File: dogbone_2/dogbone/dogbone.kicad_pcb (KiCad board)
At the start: 2 copper layers, 23 x 27.4 mm, 11 parts, among them J1 jstsh5x1, U1 TLV2771CDBVT

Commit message: added more to the mainboard/daugher board
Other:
- board text added: "ALT"
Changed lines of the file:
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@@
   (general
     (thickness 1.6)
-    (drawings 4)
+    (drawings 5)
     (tracks 53)
     (zones 0)
@@
     (37 F.SilkS user)
     (38 B.Mask user)
-    (39 F.Mask user hide)
+    (39 F.Mask user)
     (40 Dwgs.User user)
     (41 Cmts.User user)
@@
       (effects (font (size 1 1) (thickness 0.15)) (justify mirror))
     )
+    (fp_line (start -4.805 -6.84) (end 3.185 -6.84) (layer Dwgs.User) (width 0.12))
+    (fp_line (start -4.805 -6.84) (end -4.805 -3) (layer Dwgs.User) (width 0.12))
+    (fp_line (start 3.185 -3) (end -4.805 -3) (layer Dwgs.User) (width 0.12))
     (fp_line (start 3.185 -3) (end 3.185 -6.84) (layer Dwgs.User) (width 0.12))
-    (fp_line (start 3.185 -3) (end -4.805 -3) (layer Dwgs.User) (width 0.12))
-    (fp_line (start -4.805 -6.84) (end -4.805 -3) (layer Dwgs.User) (width 0.12))
-    (fp_line (start -4.805 -6.84) (end 3.185 -6.84) (layer Dwgs.User) (width 0.12))
     (pad 5 smd rect (at 1.19 -2.54 180) (size 0.6 1.55) (layers B.Cu B.Paste B.Mask)
       (net 4 "Net-(J1-Pad5)"))
@@
     (pad 1 thru_hole circle (at -0.007 9.175) (size 2.5 2.5) (drill 2) (layers *.Cu *.Mask))
   )
+  (gr_text ALT (at 64.6176 78.486) (layer F.SilkS)
+    (effects (font (size 1.5 1.5) (thickness 0.3)))
+  )
   (gr_line (start 67.577 76.073) (end 67.577 103.427) (layer Edge.Cuts) (width 0.05))

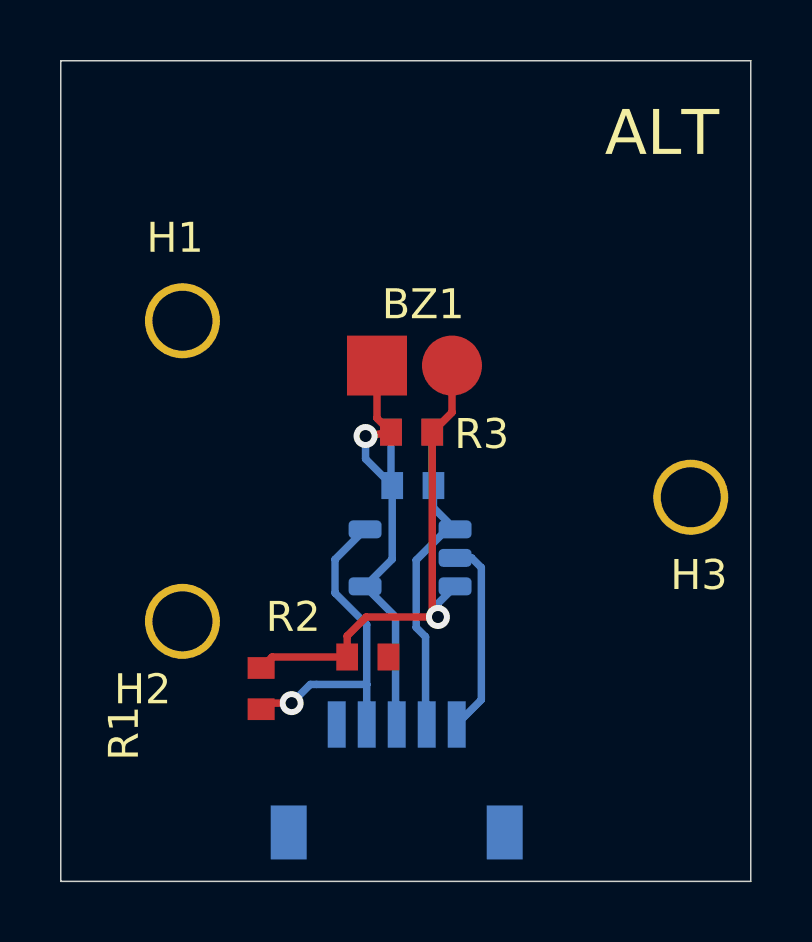
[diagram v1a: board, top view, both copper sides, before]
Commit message: fixed dogbones
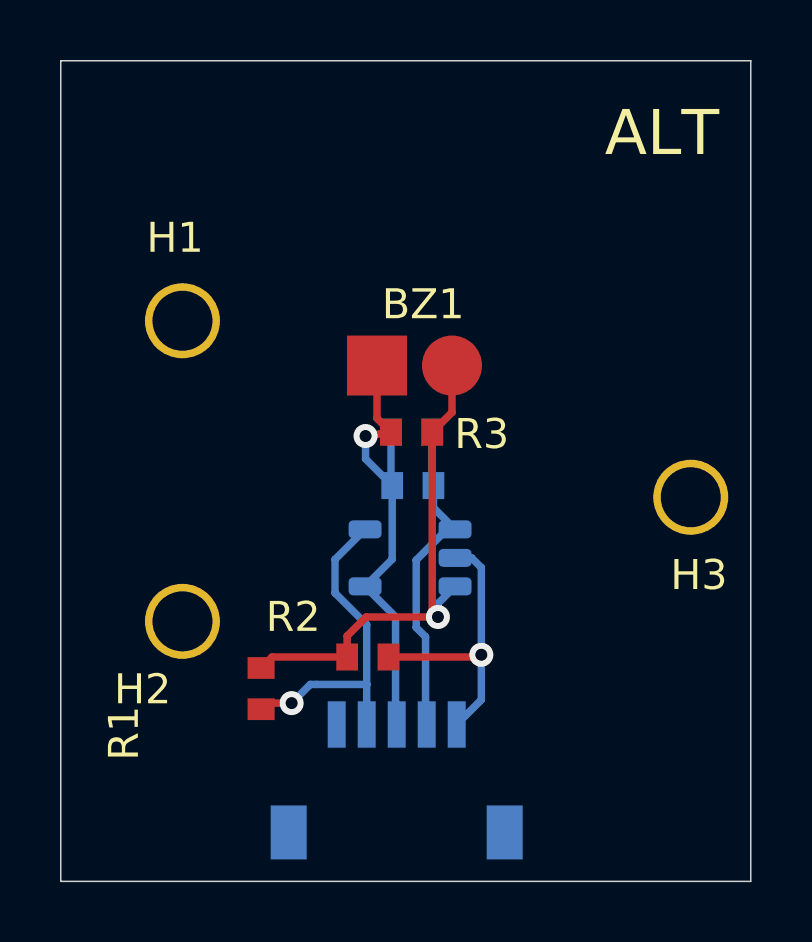
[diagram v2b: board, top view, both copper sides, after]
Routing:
- net GND: track 6.58 -> 9.71 mm, vias 0 -> 1
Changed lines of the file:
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@@
     (thickness 1.6)
     (drawings 5)
-    (tracks 53)
+    (tracks 57)
     (zones 0)
     (modules 11)
@@
       (effects (font (size 1 1) (thickness 0.15)) (justify mirror))
     )
+    (fp_line (start 3.185 -3) (end 3.185 -6.84) (layer Dwgs.User) (width 0.12))
+    (fp_line (start 3.185 -3) (end -4.805 -3) (layer Dwgs.User) (width 0.12))
+    (fp_line (start -4.805 -6.84) (end -4.805 -3) (layer Dwgs.User) (width 0.12))
     (fp_line (start -4.805 -6.84) (end 3.185 -6.84) (layer Dwgs.User) (width 0.12))
-    (fp_line (start -4.805 -6.84) (end -4.805 -3) (layer Dwgs.User) (width 0.12))
-    (fp_line (start 3.185 -3) (end -4.805 -3) (layer Dwgs.User) (width 0.12))
-    (fp_line (start 3.185 -3) (end 3.185 -6.84) (layer Dwgs.User) (width 0.12))
     (pad 5 smd rect (at 1.19 -2.54 180) (size 0.6 1.55) (layers B.Cu B.Paste B.Mask)
       (net 4 "Net-(J1-Pad5)"))
@@
   (segment (start 54.737 88.5825) (end 54.864 88.4555) (width 0.25) (layer F.Cu) (net 2))
   (via (at 54.737 88.5825) (size 0.8) (drill 0.4) (layers F.Cu B.Cu) (net 2))
-  (segment (start 54.737 89.3445) (end 55.626 90.2335) (width 0.25) (layer B.Cu) (net 2))
-  (segment (start 54.737 88.5825) (end 54.737 89.3445) (width 0.25) (layer B.Cu) (net 2))
   (segment (start 55.7375 98.1583) (end 55.7756 98.1964) (width 0.25) (layer B.Cu) (net 2))
   (segment (start 55.7375 94.61) (end 55.7375 98.1583) (width 0.25) (layer B.Cu) (net 2))
+  (segment (start 54.737 88.5825) (end 54.737 89.3445) (width 0.25) (layer B.Cu) (net 2))
+  (segment (start 54.737 89.3445) (end 55.626 90.2335) (width 0.25) (layer B.Cu) (net 2))
   (segment (start 56.9595 90.192) (end 57.001 90.2335) (width 0.25) (layer B.Cu) (net 3))
   (segment (start 56.9595 88.4555) (end 56.9595 90.192) (width 0.25) (layer B.Cu) (net 3))
@@
   (segment (start 58.59651 92.96901) (end 58.2715 92.644) (width 0.25) (layer B.Cu) (net 6))
   (segment (start 58.59651 97.37549) (end 57.7756 98.1964) (width 0.25) (layer B.Cu) (net 6))
-  (segment (start 58.59651 92.96901) (end 58.59651 97.37549) (width 0.25) (layer B.Cu) (net 6))
+  (segment (start 58.59651 92.96901) (end 58.59651 95.87359) (width 0.25) (layer B.Cu) (net 6))
+  (segment (start 58.59651 95.87359) (end 58.59651 97.37549) (width 0.25) (layer B.Cu) (net 6))
+  (via (at 58.59651 95.87359) (size 0.8) (drill 0.4) (layers F.Cu B.Cu) (net 6))
+  (segment (start 58.5216 95.9485) (end 58.59651 95.87359) (width 0.25) (layer F.Cu) (net 6))
+  (segment (start 55.499 95.9485) (end 58.5216 95.9485) (width 0.25) (layer F.Cu) (net 6))
 )
